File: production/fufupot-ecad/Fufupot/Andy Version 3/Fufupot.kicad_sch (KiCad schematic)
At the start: 62 parts, among them IC1 FOD3150, J1 Conn_01x04, J1 USB_B, J10 Conn_01x03, J11 Conn_01x03, J12 Conn_01x02, J13 Conn_01x03, J3 Conn_01x03, J4 Conn_01x02, J6 Conn_01x02, J7 Conn_01x02, J8 Conn_01x04, J9 Conn_01x02, SW1 SW_Push, U1 STGP8NC60KD, U2 FT232RL, U2 LM5165DRC, U3 USBLC6-2SC6, U4 ATMEGA328P-PN

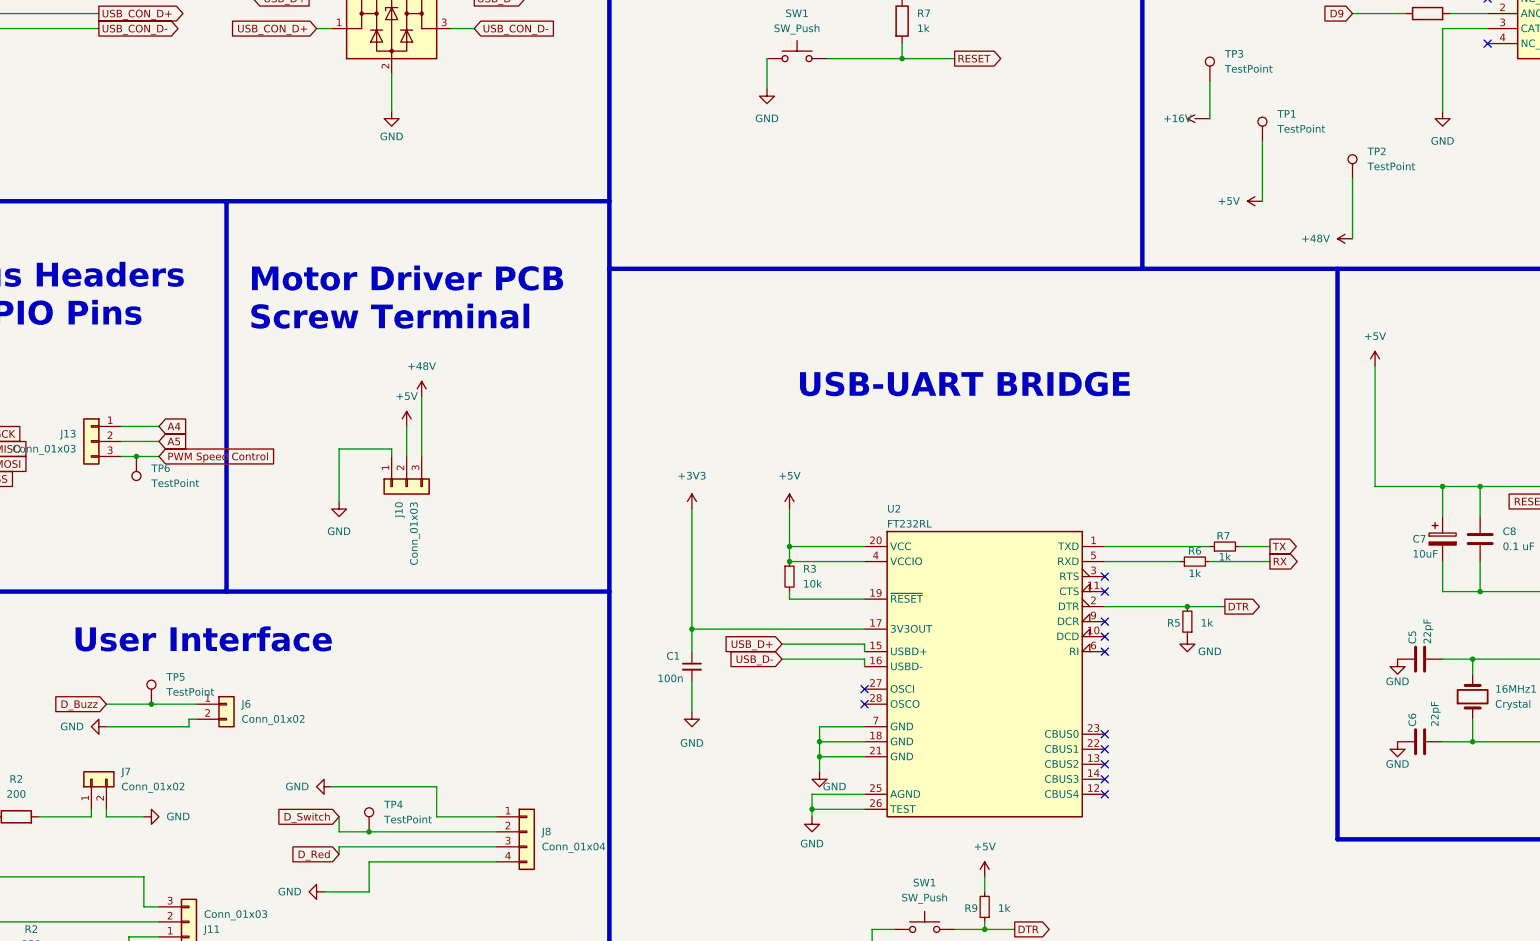
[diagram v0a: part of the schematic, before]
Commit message: Added testpoints
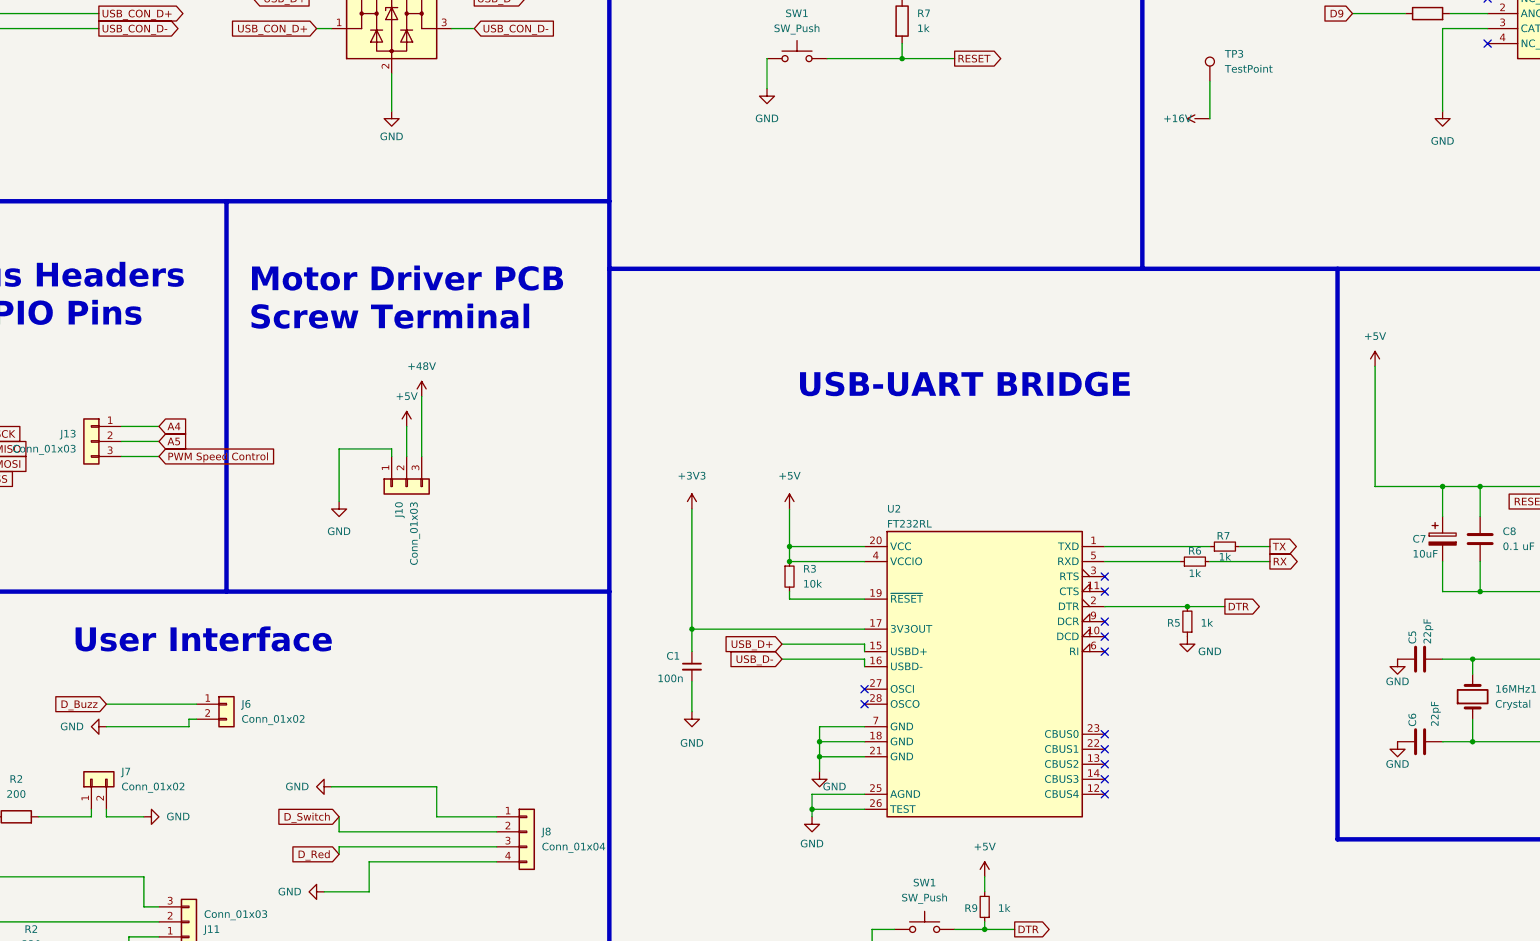
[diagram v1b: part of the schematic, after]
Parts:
- removed TP1, TP2, TP4, TP5, TP6: TestPoint, TestPoint:TestPoint_Pad_2.0x2.0mm, symbol Connector:TestPoint
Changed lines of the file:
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@@
     (comment 3 "Engineers: Katie Dewhurst, Catherine Menten, Luis Rodriguez")
   )
-  (junction (at 60.96 187.96) (diameter 0) (color 0 0 0 0)
-  )
   (junction (at 370.84 85.09) (diameter 0) (color 0 0 0 0)
   )
@@
   (junction (at 175.26 247.65) (diameter 0) (color 0 0 0 0)
   )
-  (junction (at 63.5 229.87) (diameter 0) (color 0 0 0 0)
-  )
   (junction (at 331.47 134.62) (diameter 0) (color 0 0 0 0)
   )
@@
   (junction (at 303.53 193.04) (diameter 0) (color 0 0 0 0)
   )
-  (junction (at 100.33 251.46) (diameter 0) (color 0 0 0 0)
-  )
   (junction (at 121.92 35.56) (diameter 0) (color 0 0 0 0)
   )
@@
     (stroke (width 0) (type default))
   )
-  (wire (pts (xy 251.46 134.62) (xy 251.46 144.78))
-    (stroke (width 0) (type default))
-  )
   (wire (pts (xy 44.45 248.92) (xy 53.34 248.92))
     (stroke (width 0) (type default))
@@
     (stroke (width 0) (type default))
   )
-  (wire (pts (xy 60.96 187.96) (xy 64.77 187.96))
-    (stroke (width 0) (type default))
-  )
   (wire (pts (xy 346.71 121.92) (xy 346.71 125.73))
     (stroke (width 0) (type default))
@@
     (stroke (width 0) (type default))
   )
-  (wire (pts (xy 58.42 187.96) (xy 60.96 187.96))
+  (wire (pts (xy 58.42 187.96) (xy 64.77 187.96))
     (stroke (width 0) (type default))
   )
@@
     (stroke (width 0) (type default))
   )
-  (wire (pts (xy 266.7 140.97) (xy 266.7 151.13))
-    (stroke (width 0) (type default))
-  )
   (wire (pts (xy 46.99 60.96) (xy 46.99 58.42))
     (stroke (width 0) (type default))
@@
     (stroke (width 0) (type default))
   )
-  (wire (pts (xy 95.25 251.46) (xy 100.33 251.46))
+  (wire (pts (xy 95.25 251.46) (xy 121.92 251.46))
     (stroke (width 0) (type default))
   )
@@
     (stroke (width 0) (type default))
   )
-  (wire (pts (xy 55.88 229.87) (xy 63.5 229.87))
+  (wire (pts (xy 55.88 229.87) (xy 71.12 229.87))
     (stroke (width 0) (type default))
   )
@@
     (stroke (width 0) (type default))
   )
-  (wire (pts (xy 100.33 251.46) (xy 121.92 251.46))
-    (stroke (width 0) (type default))
-  )
   (wire (pts (xy 281.94 236.22) (xy 287.02 236.22))
     (stroke (width 0) (type default))
@@
     (stroke (width 0) (type default))
   )
-  (wire (pts (xy 63.5 229.87) (xy 71.12 229.87))
-    (stroke (width 0) (type default))
-  )
   (wire (pts (xy 386.08 226.06) (xy 375.92 226.06))
     (stroke (width 0) (type default))
@@
     )
   )
-  (symbol (lib_id "Connector:TestPoint") (at 251.46 134.62 0) (unit 1)
-    (in_bom yes) (on_board yes) (dnp no) (fields_autoplaced)
-    (property "Reference" "TP1" (at 254 130.048 0)
-      (effects (font (size 1.27 1.27)) (justify left))
-    )
-    (property "Value" "TestPoint" (at 254 132.588 0)
-      (effects (font (size 1.27 1.27)) (justify left))
-    )
-    (property "Footprint" "TestPoint:TestPoint_Pad_2.0x2.0mm" (at 256.54 134.62 0)
-      (effects (font (size 1.27 1.27)) hide)
-    )
-    (property "Datasheet" "~" (at 256.54 134.62 0)
-      (effects (font (size 1.27 1.27)) hide)
-    )
-    (pin "1")
-    (instances
-      (project "Fufupot"
-        (path "/e8bc21b1-eda8-45a8-be25-55b90339183f"
-          (reference "TP1") (unit 1)
-        )
-      )
-    )
-  )
   (symbol (lib_id "Device:C") (at 96.52 43.18 0) (unit 1)
     (in_bom yes) (on_board yes) (dnp no) (fields_autoplaced)
@@
     )
   )
-  (symbol (lib_id "Connector:TestPoint") (at 60.96 187.96 180) (unit 1)
-    (in_bom yes) (on_board yes) (dnp no) (fields_autoplaced)
-    (property "Reference" "TP6" (at 63.5 189.992 0)
-      (effects (font (size 1.27 1.27)) (justify right))
-    )
-    (property "Value" "TestPoint" (at 63.5 192.532 0)
-      (effects (font (size 1.27 1.27)) (justify right))
-    )
-    (property "Footprint" "TestPoint:TestPoint_Pad_2.0x2.0mm" (at 55.88 187.96 0)
-      (effects (font (size 1.27 1.27)) hide)
-    )
-    (property "Datasheet" "~" (at 55.88 187.96 0)
-      (effects (font (size 1.27 1.27)) hide)
-    )
-    (pin "1")
-    (instances
-      (project "Fufupot"
-        (path "/e8bc21b1-eda8-45a8-be25-55b90339183f"
-          (reference "TP6") (unit 1)
-        )
-      )
-    )
-  )
   (symbol (lib_id "power:+3V3") (at 154.94 196.85 0) (unit 1)
     (in_bom yes) (on_board yes) (dnp no) (fields_autoplaced)
@@
     )
   )
-  (symbol (lib_id "power:+48V") (at 266.7 151.13 90) (unit 1)
-    (in_bom yes) (on_board yes) (dnp no) (fields_autoplaced)
-    (property "Reference" "#PWR048" (at 270.51 151.13 0)
-      (effects (font (size 1.27 1.27)) hide)
-    )
-    (property "Value" "+48V" (at 262.89 151.13 90)
-      (effects (font (size 1.27 1.27)) (justify left))
-    )
-    (property "Footprint" "" (at 266.7 151.13 0)
-      (effects (font (size 1.27 1.27)) hide)
-    )
-    (property "Datasheet" "" (at 266.7 151.13 0)
-      (effects (font (size 1.27 1.27)) hide)
-    )
-    (pin "1")
-    (instances
-      (project "Fufupot"
-        (path "/e8bc21b1-eda8-45a8-be25-55b90339183f"
-          (reference "#PWR048") (unit 1)
-        )
-      )
-    )
-  )
   (symbol (lib_id "power:GND") (at 167.64 125.73 0) (unit 1)
     (in_bom yes) (on_board yes) (dnp no) (fields_autoplaced)
@@
     )
   )
-  (symbol (lib_id "Connector:TestPoint") (at 63.5 229.87 0) (unit 1)
-    (in_bom yes) (on_board yes) (dnp no) (fields_autoplaced)
-    (property "Reference" "TP5" (at 66.04 225.298 0)
-      (effects (font (size 1.27 1.27)) (justify left))
-    )
-    (property "Value" "TestPoint" (at 66.04 227.838 0)
-      (effects (font (size 1.27 1.27)) (justify left))
-    )
-    (property "Footprint" "TestPoint:TestPoint_Pad_2.0x2.0mm" (at 68.58 229.87 0)
-      (effects (font (size 1.27 1.27)) hide)
-    )
-    (property "Datasheet" "~" (at 68.58 229.87 0)
-      (effects (font (size 1.27 1.27)) hide)
-    )
-    (pin "1")
-    (instances
-      (project "Fufupot"
-        (path "/e8bc21b1-eda8-45a8-be25-55b90339183f"
-          (reference "TP5") (unit 1)
-        )
-      )
-    )
-  )
   (symbol (lib_id "Device:R_Small") (at 240.03 205.74 90) (unit 1)
     (in_bom yes) (on_board yes) (dnp no)
@@
     )
   )
-  (symbol (lib_id "Connector:TestPoint") (at 266.7 140.97 0) (unit 1)
-    (in_bom yes) (on_board yes) (dnp no) (fields_autoplaced)
-    (property "Reference" "TP2" (at 269.24 136.398 0)
-      (effects (font (size 1.27 1.27)) (justify left))
-    )
-    (property "Value" "TestPoint" (at 269.24 138.938 0)
-      (effects (font (size 1.27 1.27)) (justify left))
-    )
-    (property "Footprint" "TestPoint:TestPoint_Pad_2.0x2.0mm" (at 271.78 140.97 0)
-      (effects (font (size 1.27 1.27)) hide)
-    )
-    (property "Datasheet" "~" (at 271.78 140.97 0)
-      (effects (font (size 1.27 1.27)) hide)
-    )
-    (pin "1")
-    (instances
-      (project "Fufupot"
-        (path "/e8bc21b1-eda8-45a8-be25-55b90339183f"
-          (reference "TP2") (unit 1)
-        )
-      )
-    )
-  )
   (symbol (lib_id "Device:R") (at 271.78 40.64 0) (unit 1)
     (in_bom yes) (on_board yes) (dnp no) (fields_autoplaced)
@@
     )
   )
-  (symbol (lib_id "power:+5V") (at 251.46 144.78 90) (unit 1)
-    (in_bom yes) (on_board yes) (dnp no) (fields_autoplaced)
-    (property "Reference" "#PWR049" (at 255.27 144.78 0)
-      (effects (font (size 1.27 1.27)) hide)
-    )
-    (property "Value" "+5V" (at 247.65 144.78 90)
-      (effects (font (size 1.27 1.27)) (justify left))
-    )
-    (property "Footprint" "" (at 251.46 144.78 0)
-      (effects (font (size 1.27 1.27)) hide)
-    )
-    (property "Datasheet" "" (at 251.46 144.78 0)
-      (effects (font (size 1.27 1.27)) hide)
-    )
-    (pin "1")
-    (instances
-      (project "Fufupot"
-        (path "/e8bc21b1-eda8-45a8-be25-55b90339183f"
-          (reference "#PWR049") (unit 1)
-        )
-      )
-    )
-  )
   (symbol (lib_id "Device:R") (at 40.64 248.92 90) (unit 1)
     (in_bom yes) (on_board yes) (dnp no) (fields_autoplaced)
@@
         )
       )
-    )
-  )
-  (symbol (lib_id "Connector:TestPoint") (at 100.33 251.46 0) (unit 1)
-    (in_bom yes) (on_board yes) (dnp no) (fields_autoplaced)
-    (property "Reference" "TP4" (at 102.87 246.888 0)
-      (effects (font (size 1.27 1.27)) (justify left))
-    )
-    (property "Value" "TestPoint" (at 102.87 249.428 0)
-      (effects (font (size 1.27 1.27)) (justify left))
-    )
-    (property "Footprint" "TestPoint:TestPoint_Pad_2.0x2.0mm" (at 105.41 251.46 0)
-      (effects (font (size 1.27 1.27)) hide)
-    )
-    (property "Datasheet" "~" (at 105.41 251.46 0)
-      (effects (font (size 1.27 1.27)) hide)
-    )
-    (pin "1")
-    (instances
-      (project "Fufupot"
-        (path "/e8bc21b1-eda8-45a8-be25-55b90339183f"
-          (reference "TP4") (unit 1)
-        )
-      )
